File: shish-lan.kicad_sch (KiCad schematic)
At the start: 8 parts

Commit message: top level clean up. Refs: #1
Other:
- sheet switch ports: added none; removed 1V15_EN, 25M_CLK_SWITCH, EN-1V15_STM_TO_BUCK, EN-2V5_STM_TO_BUCK, EN-3V3_STM_TO_BUCK
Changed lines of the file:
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@@
 		(exclude_from_sim no)
 		(at 185.42 27.94 0)
-		(size 58.42 12.7)
+		(size 30.48 12.7)
 		(margins 0.9525 0.9525 0.9525 0.9525)
 		(stroke
@@
 	(text_box "PTP3 is shared with IRQ0, but not at the same time. A 0R is taking care of it."
 		(exclude_from_sim no)
-		(at 124.46 113.03 0)
-		(size 58.42 12.7)
+		(at 217.17 27.94 0)
+		(size 45.72 12.7)
 		(margins 0.9525 0.9525 0.9525 0.9525)
 		(stroke
@@
 	(bus
 		(pts
-			(xy 95.25 73.66) (xy 185.42 73.66)
+			(xy 95.25 55.88) (xy 185.42 55.88)
 		)
 		(stroke
@@
 		)
 	)
+	(wire
+		(pts
+			(xy 95.25 60.96) (xy 185.42 60.96)
+		)
+		(stroke
+			(width 0)
+			(type default)
+		)
+	)
 	(bus
 		(pts
@@
 	(bus
 		(pts
-			(xy 95.25 71.12) (xy 185.42 71.12)
+			(xy 95.25 53.34) (xy 185.42 53.34)
 		)
 		(stroke
@@
 	(wire
 		(pts
-			(xy 95.25 92.71) (xy 185.42 92.71)
+			(xy 95.25 64.77) (xy 185.42 64.77)
 		)
 		(stroke
@@
 	(bus
 		(pts
-			(xy 95.25 68.58) (xy 185.42 68.58)
+			(xy 95.25 50.8) (xy 185.42 50.8)
 		)
 		(stroke
@@
 		)
 		(pin "EN-1V15_STM_TO_BUCK" output
-			(at 95.25 41.91 0)
+			(at 95.25 68.58 0)
 			(effects
 				(font
@@
 		)
 		(pin "EN-2V5_STM_TO_BUCK" output
-			(at 95.25 44.45 0)
+			(at 95.25 71.12 0)
 			(effects
 				(font
@@
 		)
 		(pin "EN-3V3_STM_TO_BUCK" output
-			(at 95.25 46.99 0)
+			(at 95.25 73.66 0)
 			(effects
 				(font
@@
 		)
 		(pin "IRQ0_SWITCH_TO_STM" input
-			(at 95.25 49.53 0)
+			(at 95.25 60.96 0)
 			(effects
 				(font
@@
 		)
 		(pin "MIIM_STM_SWITCH{MDIO,MDC}" bidirectional
-			(at 95.25 71.12 0)
+			(at 95.25 53.34 0)
 			(effects
 				(font
@@
 		)
 		(pin "nRST_STM_TO_SWITCH" output
-			(at 95.25 92.71 0)
+			(at 95.25 64.77 0)
 			(effects
 				(font
@@
 		(pin "RGMII1_SWITCH_STM{TXD[0..3], TX_CLK, TX_CTLR, RXD[0..3], RX_CLK, RX_CTLR}"
 			bidirectional
-			(at 95.25 68.58 0
+			(at 95.25 50.8 0
 			)
 			(effects
@@
 		)
 		(pin "SPI_STM_SWITCH{MOSI,MISO,nCS,CLK}" bidirectional
-			(at 95.25 73.66 0)
+			(at 95.25 55.88 0)
 			(effects
 				(font
@@
 	(sheet
 		(at 185.42 44.45)
-		(size 77.47 82.55)
+		(size 77.47 24.13)
 		(exclude_from_sim no)
 		(in_bom yes)
@@
 		)
 		(property "Sheetfile" "switch.kicad_sch"
-			(at 185.42 127.5846 0)
+			(at 185.42 69.1646 0)
 			(effects
 				(font
@@
 			)
 		)
-		(pin "1V15_EN" input
-			(at 185.42 50.8 180)
-			(effects
-				(font
-					(size 1.27 1.27)
-				)
-				(justify left)
-			)
-		)
 		(pin "RGMII1_SWITCH_STM{TXD[0..3], TX_CLK, TX_CTLR, RXD[0..3], RX_CLK, RX_CTLR}"
 			bidirectional
-			(at 185.42 68.58 180
+			(at 185.42 50.8 180
 			)
 			(effects
@@
 		)
 		(pin "MIIM_STM_SWITCH{MDIO,MDC}" bidirectional
-			(at 185.42 71.12 180)
+			(at 185.42 53.34 180)
 			(effects
 				(font
@@
 		)
 		(pin "nRST_STM_TO_SWITCH" input
-			(at 185.42 92.71 180)
-			(effects
-				(font
-					(size 1.27 1.27)
-				)
-				(justify left)
-			)
-		)
-		(pin "25M_CLK_SWITCH" input
-			(at 185.42 95.25 180)
+			(at 185.42 64.77 180)
 			(effects
 				(font
@@
 		)
 		(pin "SPI_STM_SWITCH{MOSI,MISO,nCS,CLK}" bidirectional
-			(at 185.42 73.66 180)
-			(effects
-				(font
-					(size 1.27 1.27)
-				)
-				(justify left)
-			)
-		)
-		(pin "CLK-25M_OSC" input
 			(at 185.42 55.88 180)
 			(effects
@@
 			)
 		)
-		(pin "EN-2V5_STM_TO_BUCK" input
-			(at 185.42 101.6 180)
-			(effects
-				(font
-					(size 1.27 1.27)
-				)
-				(justify left)
-			)
-		)
-		(pin "EN-3V3_STM_TO_BUCK" input
-			(at 185.42 97.79 180)
-			(effects
-				(font
-					(size 1.27 1.27)
-				)
-				(justify left)
-			)
-		)
-		(pin "EN-1V15_STM_TO_BUCK" input
-			(at 185.42 104.14 180)
+		(pin "CLK-25M_OSC" input
+			(at 185.42 46.99 180)
 			(effects
 				(font
@@
 		)
 		(pin "IRQ0_SWITCH_TO_STM" output
-			(at 185.42 82.55 180)
+			(at 185.42 60.96 180)
 			(effects
 				(font

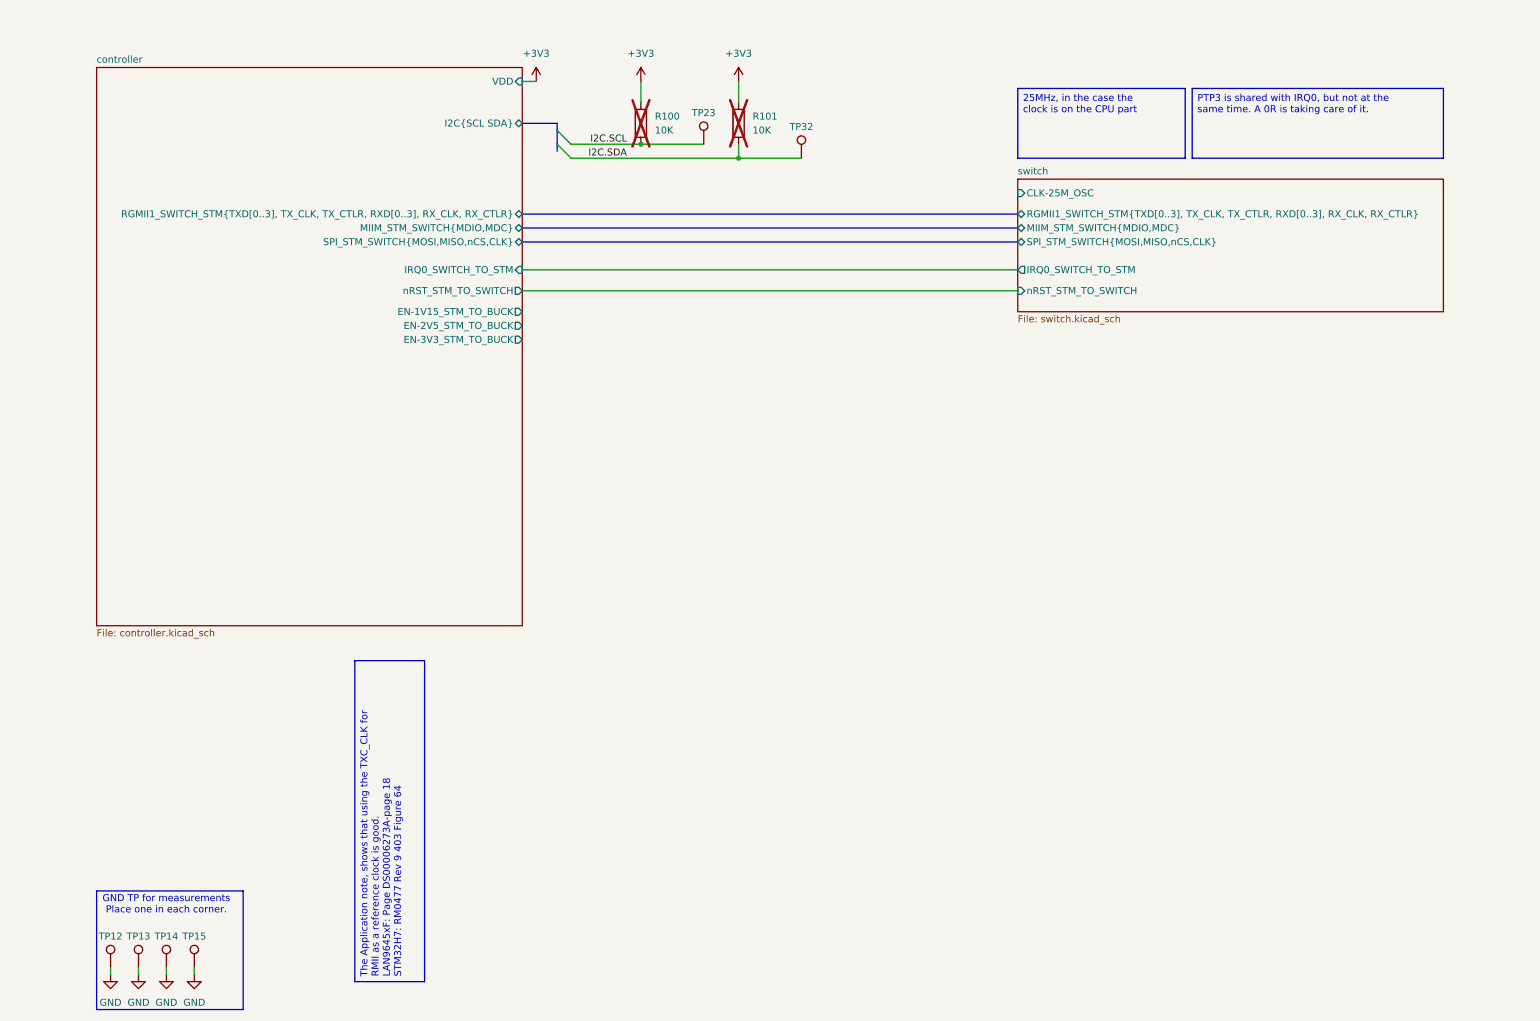
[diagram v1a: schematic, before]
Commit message: Uses crystal sheet in all places. Refs: #1
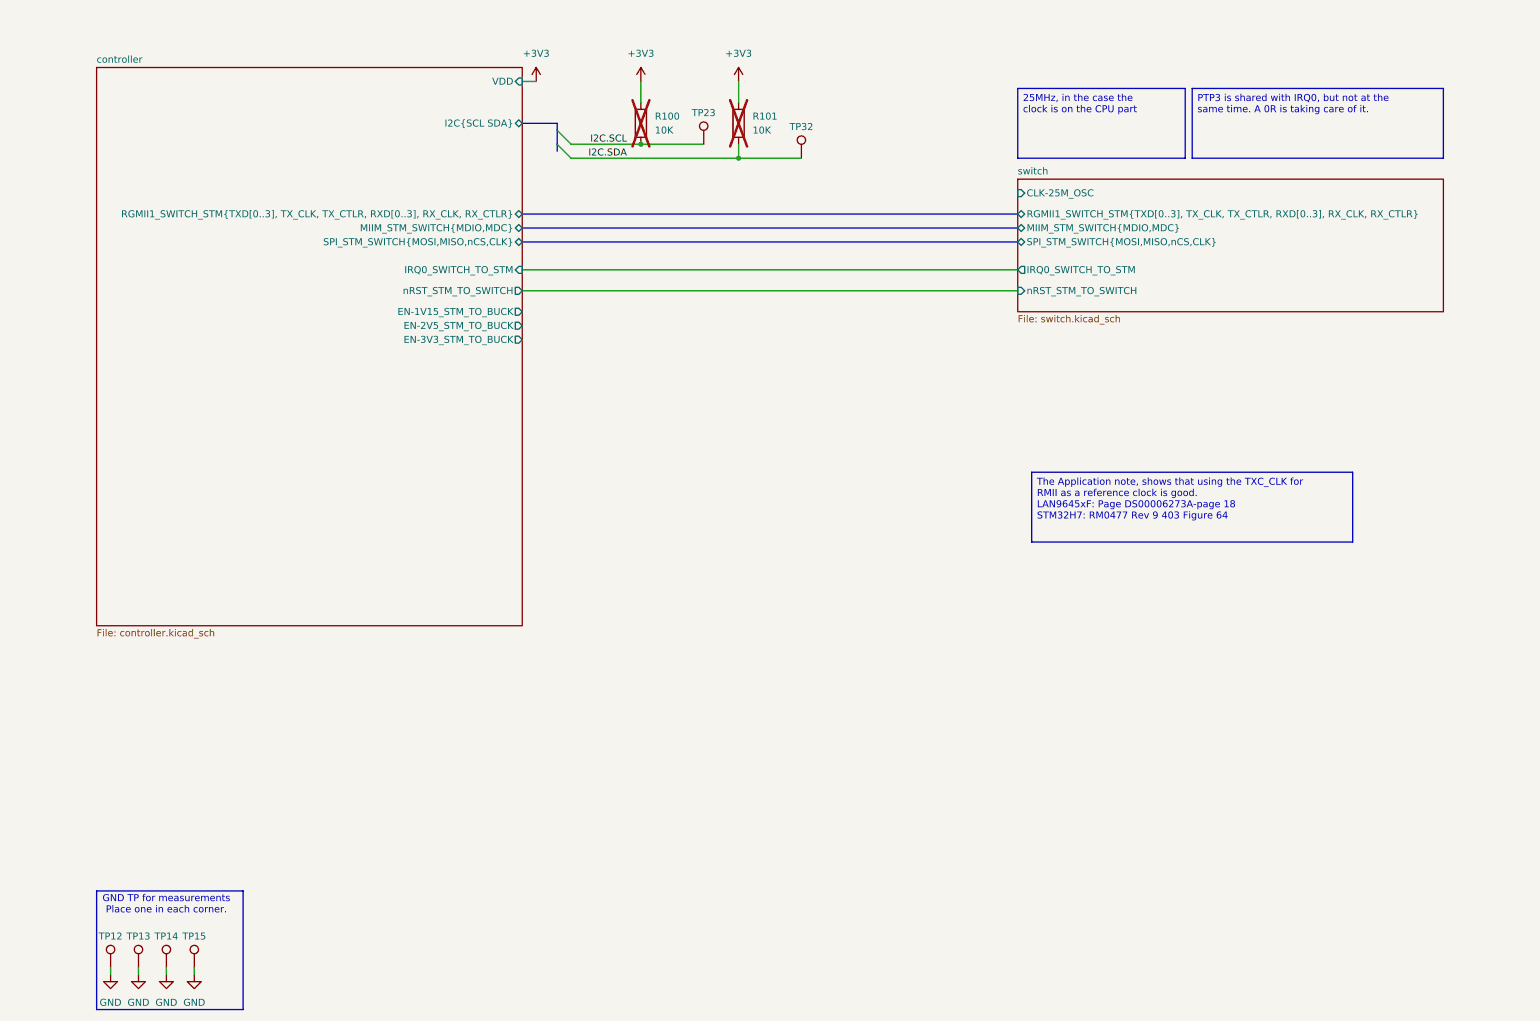
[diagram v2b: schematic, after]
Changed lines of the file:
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@@
 	(text_box "The Application note, shows that using the TXC_CLK for RMII as a reference clock is good.\nLAN9645xF: Page DS00006273A-page 18\nSTM32H7: RM0477 Rev 9 403 Figure 64\n"
 		(exclude_from_sim no)
-		(at 64.77 132.08 90)
-		(size 12.7 58.42)
+		(at 187.96 97.79 0)
+		(size 58.42 12.7)
 		(margins 0.9525 0.9525 0.9525 0.9525)
 		(stroke
@@
 	)
 	(image
-		(at 114.3 176.53)
+		(at 224.79 133.35)
 		(scale 0.429341)
 		(data "iVBORw0KGgoAAAANSUhEUgAAB+wAAARbCAIAAAAiCs8eAAAAA3NCSVQICAjb4U/gAAAgAElEQVR4"
@@
 	)
 	(image
-		(at 104.14 140.97)
+		(at 236.22 83.82)
 		(scale 0.456643)
 		(data "iVBORw0KGgoAAAANSUhEUgAABX0AAAKgCAIAAABIiknoAAAAA3NCSVQICAjb4U/gAAAgAElEQVR4"

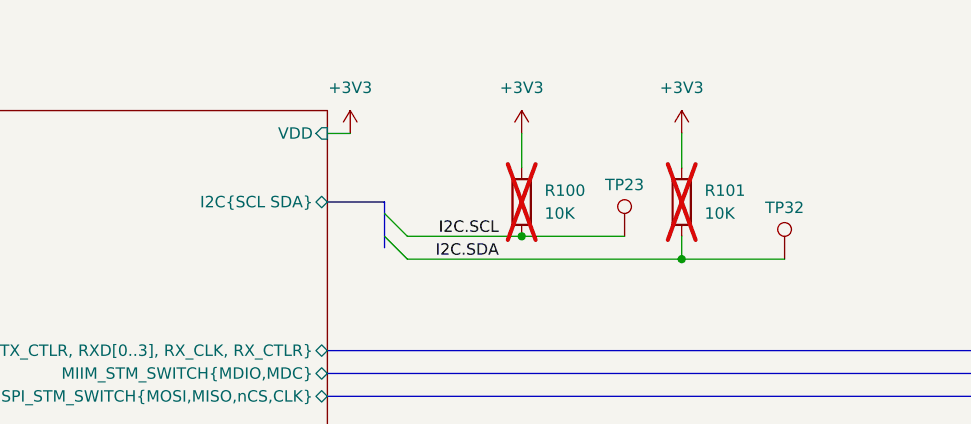
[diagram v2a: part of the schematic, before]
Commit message: renames I2C to I2C1. Refs: #1
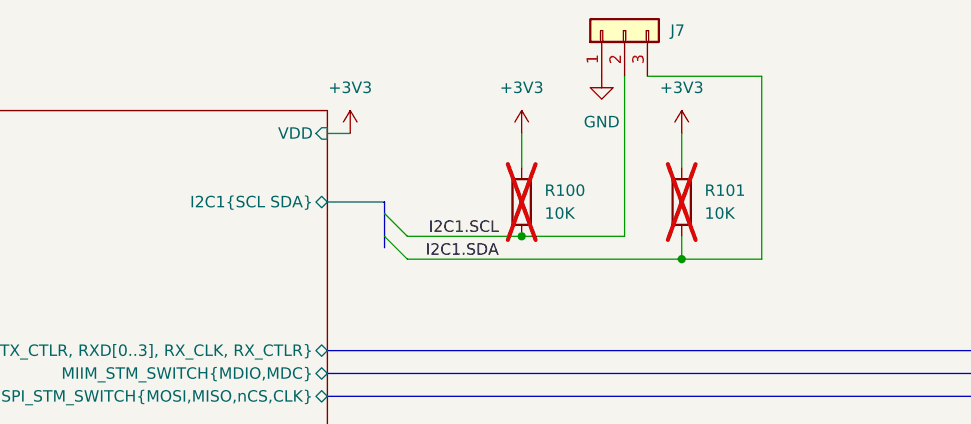
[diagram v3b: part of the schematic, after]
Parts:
- removed TP23, TP32: ~, Connector_PinHeader_2.54mm:PinHeader_1x01_P2.54mm_Vertical, symbol KL_TP:TestPoint
- added J7: ~, KL:03x01_2.54mm_Header, symbol KL_Headers:03x01_2.54mm_Header
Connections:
- net GND: now also J7.1 (Pin_1)
- net I2C.SCL renamed I2C1.SCL
- net I2C1.SCL: now also J7.2 (Pin_2)
- net I2C.SDA renamed I2C1.SDA
- net I2C1.SDA: now also J7.3 (Pin_3)
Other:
- sheet controller ports: added I2C1{SCL SDA}; removed I2C{SCL SDA}
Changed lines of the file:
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@@
 	(wire
 		(pts
+			(xy 143.51 40.64) (xy 134.62 40.64)
+		)
+		(stroke
+			(width 0)
+			(type default)
+		)
+	)
+	(wire
+		(pts
 			(xy 25.4 189.23) (xy 25.4 187.96)
 		)
@@
 		)
 	)
+	(bus
+		(pts
+			(xy 95.25 53.34) (xy 185.42 53.34)
+		)
+		(stroke
+			(width 0)
+			(type default)
+		)
+	)
 	(wire
 		(pts
-			(xy 134.62 40.64) (xy 146.05 40.64)
+			(xy 95.25 64.77) (xy 185.42 64.77)
 		)
 		(stroke
@@
 	(bus
 		(pts
-			(xy 95.25 53.34) (xy 185.42 53.34)
+			(xy 95.25 34.29) (xy 101.6 34.29)
 		)
 		(stroke
@@
 	(wire
 		(pts
-			(xy 95.25 64.77) (xy 185.42 64.77)
+			(xy 143.51 20.32) (xy 143.51 40.64)
 		)
 		(stroke
@@
 	(bus
 		(pts
-			(xy 95.25 34.29) (xy 101.6 34.29)
+			(xy 101.6 34.29) (xy 101.6 35.56)
 		)
 		(stroke
@@
 		)
 	)
-	(bus
+	(wire
 		(pts
-			(xy 101.6 34.29) (xy 101.6 35.56)
+			(xy 130.81 20.32) (xy 143.51 20.32)
 		)
 		(stroke
@@
 	(wire
 		(pts
+			(xy 128.27 20.32) (xy 128.27 38.1)
+		)
+		(stroke
+			(width 0)
+			(type default)
+		)
+	)
+	(wire
+		(pts
 			(xy 30.48 189.23) (xy 30.48 187.96)
 		)
@@
 		)
 	)
-	(label "I2C.SCL"
+	(label "I2C1.SCL"
 		(at 114.3 38.1 180)
 		(effects
@@
 		)
 	)
-	(label "I2C.SDA"
+	(label "I2C1.SDA"
 		(at 114.3 40.64 180)
 		(effects
@@
 	)
 	(symbol
-		(lib_id "KL_TP:TestPoint")
-		(at 128.27 38.1 0)
+		(lib_id "KL_Headers:03x01_2.54mm_Header")
+		(at 128.27 15.24 90)
 		(unit 1)
 		(exclude_from_sim no)
@@
 		(dnp no)
 		(fields_autoplaced yes)
-		(property "Reference" "TP23"
-			(at 128.27 32.385 0)
-			(do_not_autoplace yes)
+		(property "Reference" "J7"
+			(at 133.35 15.2399 90)
 			(effects
 				(font
 					(size 1.27 1.27)
 				)
+				(justify right)
 			)
 		)
 		(property "Value" "~"
-			(at 128.27 33.02 0)
+			(at 127 15.24 0)
 			(effects
 				(font
@@
 			)
 		)
-		(property "Footprint" "Connector_PinHeader_2.54mm:PinHeader_1x01_P2.54mm_Vertical"
-			(at 133.35 38.1 0)
+		(property "Footprint" "KL:03x01_2.54mm_Header"
+			(at 119.888 14.478 0)
 			(effects
 				(font
@@
 			)
 		)
-		(property "Datasheet" "~"
-			(at 133.35 38.1 0)
+		(property "Datasheet" ""
+			(at 127 15.24 0)
 			(effects
 				(font
@@
 			)
 		)
-		(property "Description" "test point"
-			(at 128.27 38.1 0)
+		(property "Description" ""
+			(at 127 15.24 0)
 			(effects
 				(font
@@
 		(pin "1"
 		)
+		(pin "3"
+		)
+		(pin "2"
+		)
 		(instances
-			(project ""
+			(project "shish-lan"
 				(path "/d4536448-b109-4159-96e2-3dc21baf2d6e"
-					(reference "TP23")
+					(reference "J7")
 					(unit 1)
 				)
@@
 	)
 	(symbol
-		(lib_id "KL_TP:TestPoint")
-		(at 146.05 40.64 0)
-		(unit 1)
-		(exclude_from_sim no)
-		(in_bom yes)
-		(on_board yes)
-		(dnp no)
-		(fields_autoplaced yes)
-		(property "Reference" "TP32"
-			(at 146.05 34.925 0)
-			(do_not_autoplace yes)
-			(effects
-				(font
-					(size 1.27 1.27)
-				)
-			)
-		)
-		(property "Value" "~"
-			(at 146.05 35.56 0)
-			(effects
-				(font
-					(size 1.27 1.27)
-				)
-				(hide yes)
-			)
-		)
-		(property "Footprint" "Connector_PinHeader_2.54mm:PinHeader_1x01_P2.54mm_Vertical"
-			(at 151.13 40.64 0)
-			(effects
-				(font
-					(size 1.27 1.27)
-				)
-				(hide yes)
-			)
-		)
-		(property "Datasheet" "~"
-			(at 151.13 40.64 0)
-			(effects
-				(font
-					(size 1.27 1.27)
-				)
-				(hide yes)
-			)
-		)
-		(property "Description" "test point"
-			(at 146.05 40.64 0)
-			(effects
-				(font
-					(size 1.27 1.27)
-				)
-				(hide yes)
-			)
-		)
-		(pin "1"
-		)
-		(instances
-			(project ""
-				(path "/d4536448-b109-4159-96e2-3dc21baf2d6e"
-					(reference "TP32")
-					(unit 1)
-				)
-			)
-		)
-	)
-	(symbol
 		(lib_id "power:+3V3")
 		(at 134.62 26.67 0)
@@
 		)
 	)
+	(symbol
+		(lib_id "KL_SYM_LOCAL:GND")
+		(at 125.73 20.32 0)
+		(unit 1)
+		(exclude_from_sim no)
+		(in_bom yes)
+		(on_board yes)
+		(dnp no)
+		(fields_autoplaced yes)
+		(property "Reference" "#PWR087"
+			(at 125.73 26.67 0)
+			(effects
+				(font
+					(size 1.27 1.27)
+				)
+				(hide yes)
+			)
+		)
+		(property "Value" "GND"
+			(at 125.73 25.4 0)
+			(effects
+				(font
+					(size 1.27 1.27)
+				)
+			)
+		)
+		(property "Footprint" ""
+			(at 125.73 20.32 0)
+			(effects
+				(font
+					(size 1.27 1.27)
+				)
+				(hide yes)
+			)
+		)
+		(property "Datasheet" ""
+			(at 125.73 20.32 0)
+			(effects
+				(font
+					(size 1.27 1.27)
+				)
+				(hide yes)
+			)
+		)
+		(property "Description" "Power symbol creates a global label with name \"GND\" , ground"
+			(at 125.73 20.32 0)
+			(effects
+				(font
+					(size 1.27 1.27)
+				)
+				(hide yes)
+			)
+		)
+		(pin "1"
+		)
+		(instances
+			(project ""
+				(path "/d4536448-b109-4159-96e2-3dc21baf2d6e"
+					(reference "#PWR087")
+					(unit 1)
+				)
+			)
+		)
+	)
 	(sheet
 		(at 17.78 24.13)
@@
 			)
 		)
-		(pin "I2C{SCL SDA}" bidirectional
+		(pin "I2C1{SCL SDA}" bidirectional
 			(at 95.25 34.29 0)
 			(effects
